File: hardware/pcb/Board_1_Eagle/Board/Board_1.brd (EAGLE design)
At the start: 81.3 x 88.9 mm, 93 parts, among them IC1 MCP73831, IC2 LT1963EST-1.5, IC3 VUB300, IC5 WTV020SD-20S, J3 DEBUG_CONNECTOR, SW1 SW_TACT_SMD, SW2 SW_TACT_SMD, SW3 SW_TACT_SMD, SW4 SW_TACT_SMD, SW5 SW_TACT_SMD, SW6 SW_TACT_SMD, SW7 SW_TACT_SMD, X1 1751248, X2 1751248, X3 1751248, Y1 CRYSTAL.3.2X2.5MM

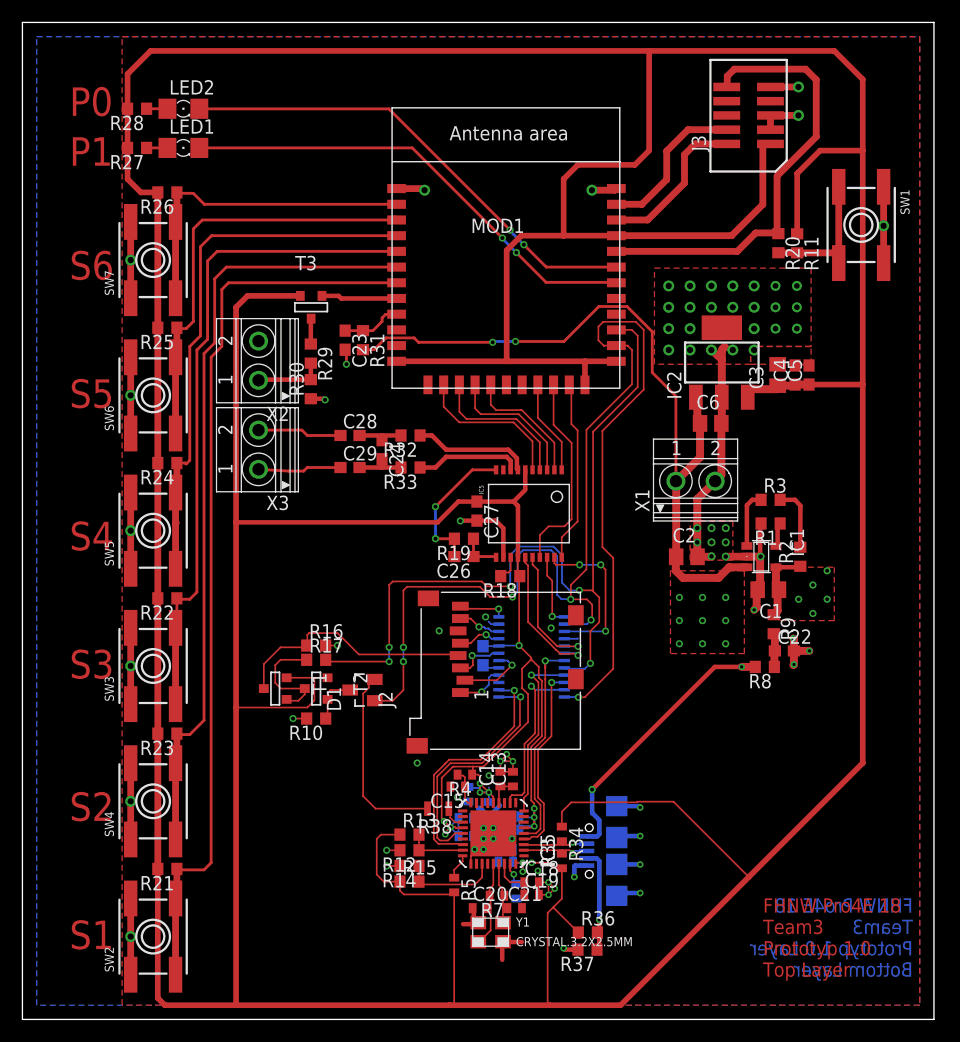
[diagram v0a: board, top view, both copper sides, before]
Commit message: Layout angepasst. Verstärker hinzugefügt
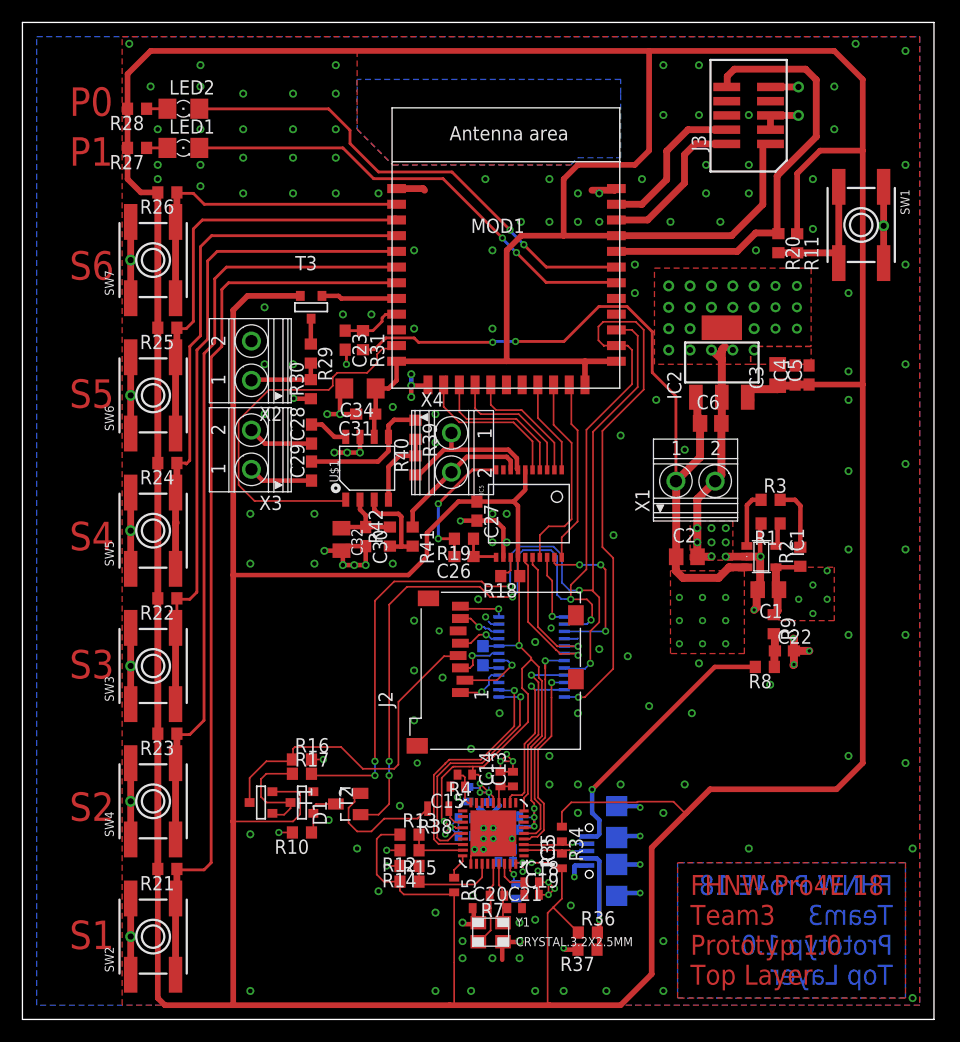
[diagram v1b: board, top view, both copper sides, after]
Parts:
- removed C24: NP, rcl:C0603
- removed R32, R33: 0R, resistor:R0603
- added C30, C31: 100n, rcl:C0603
- added C32: 1u, rcl:C0805K
- added C34: 100u, rcl:C1206
- added R39, R40, R41, R42: 1k, resistor:R0603
- added U$1: TS4890D, TI_IC:SO08-6.0
- added X4: 1751248, con-phoenix-350:1751248
- C29: value 0R -> 5.6u
- moved D1 10.2 mm to (29.1, 23.0)
- moved R10 10.2 mm to (24.9, 20.5)
- moved R16 10.2 mm to (24.9, 27.0)
- moved T1 10.2 mm to (21.3, 23.2)
- moved T2 10.2 mm to (24.9, 23.2)
- moved R17 10.2 mm to (24.9, 25.7)
- moved C29 3.44 mm to (25.8, 52.7), turned to 90 degrees
- moved C28 3.43 mm to (25.8, 56.0), turned to 90 degrees
- moved X2 0.63 mm to (20.3, 62.5)
- moved X3 0.63 mm to (20.3, 54.6)
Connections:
- removed net N$58: C24.2, C29.2, R33.2
- removed net N$59: C24.1, C28.2, R32.2
- new net N$11: C28.2, U$1.8
- new net N$12: C29.2, R39.1, U$1.5
- new net N$13: C30.1, C32.1, R42.2, U$1.2
- new net N$14: R39.2, R40.2, U$1.4
- new net N$15: R41.2, R42.1, U$1.3
- new net STANDBY: MOD1.11, U$1.1
- net +3V3: now also C31.1, C34.1, U$1.6
- net GND: now also C30.2, C31.2, C32.2, C34.2, U$1.7
- net SPK+: now also R40.1, X4.1; no longer R32.1
- net SPK-: now also R41.1, X4.2; no longer R33.1
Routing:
- net STANDBY: track 0.00 -> 34.5 mm
- net GND: track 149.1 -> 170.5 mm, vias 80 -> 233
- net N$12: track 0.00 -> 12.2 mm
- net IN: track 112.1 -> 122.7 mm
- net /EN: track 73.3 -> 83.9 mm
- net +3V3: track 653.6 -> 663.1 mm
- net NCD1: track 22.0 -> 30.8 mm
- net N$15: track 0.00 -> 8.46 mm
- net N$14: track 0.00 -> 7.22 mm
- net N$13: track 0.00 -> 7.02 mm
- net N$8: track 17.2 -> 11.4 mm
- net N$58: track 4.43 -> 0.00 mm
- net N$59: track 4.12 -> 0.00 mm
- net SPK-: track 9.43 -> 13.1 mm
- net N$11: track 0.00 -> 3.51 mm
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- added copper zone on layer 1, net N$17
- added copper zone on layer 16, net N$18
- added copper zone on layer 1, net N$68
- added copper zone on layer 16, net N$68
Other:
- board text removed: "FHNW Pro4E 18 Team3 Prototyp 1.0 Layer Bottom Layer"

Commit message: d
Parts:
- U$1: value TS4890D -> TS487ID
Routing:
- net GND: track 170.5 -> 160.9 mm, vias 233 -> 230
- net +3V3: track 663.1 -> 660.6 mm
- net N$34: track 24.5 -> 26.7 mm
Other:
- board size 81.3 x 88.9 mm -> 78.7 x 87.6 mm
- board text added: "Hergestellt aus biologisch gehaltenen Halbleitern..."

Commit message: bla
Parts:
- renumbered GND to IC30
